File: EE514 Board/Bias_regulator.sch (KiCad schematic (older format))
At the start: 12 parts

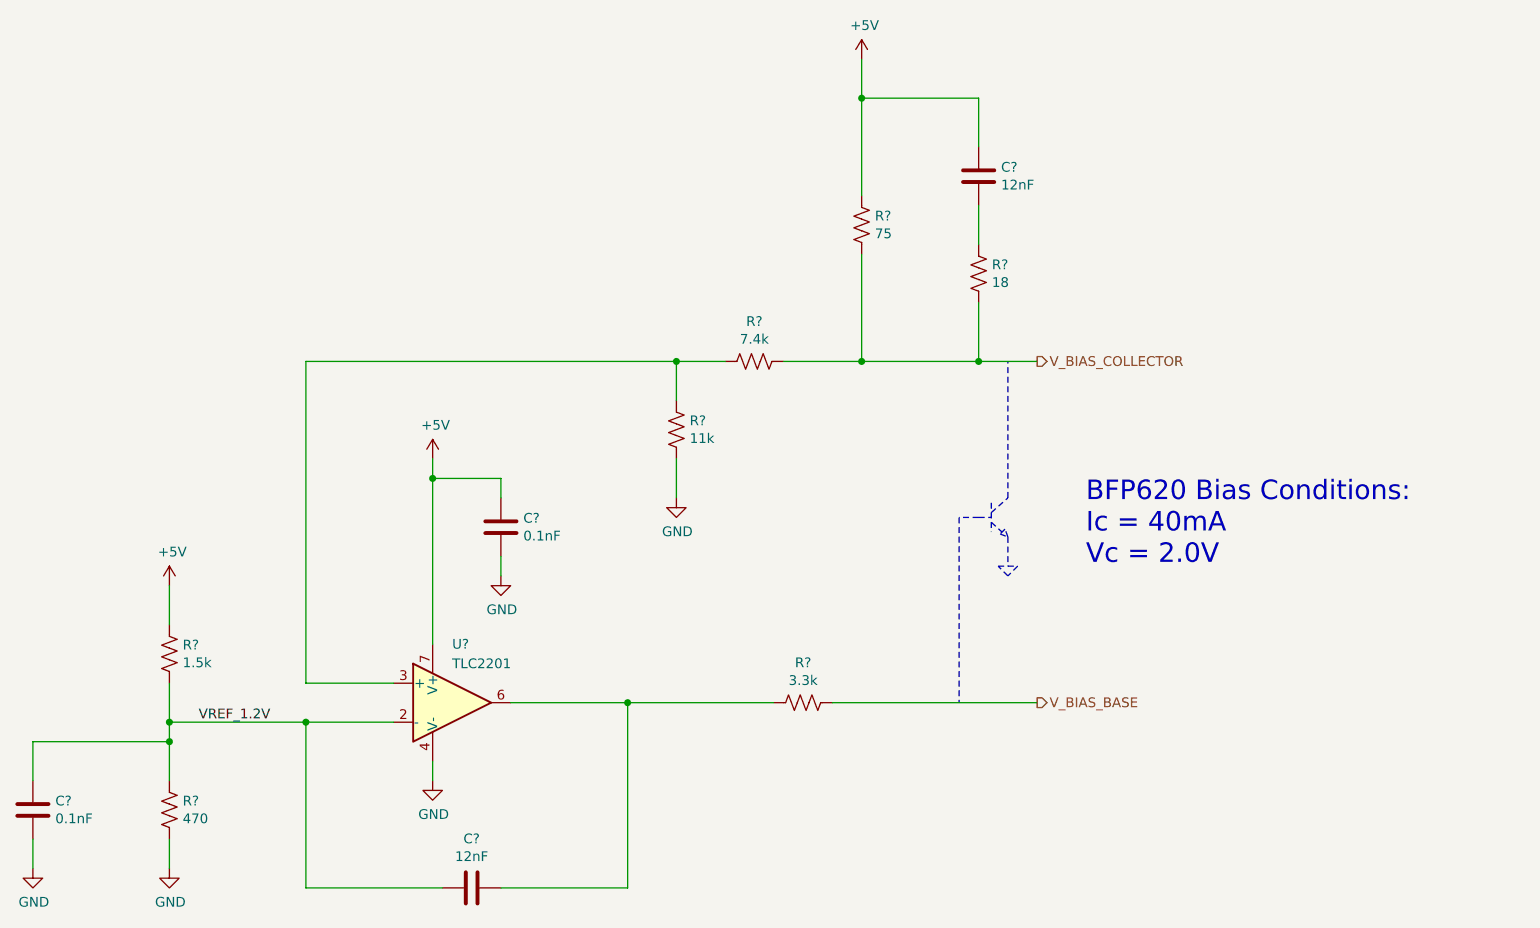
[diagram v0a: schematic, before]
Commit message: Layout finished, updating silkscreen...
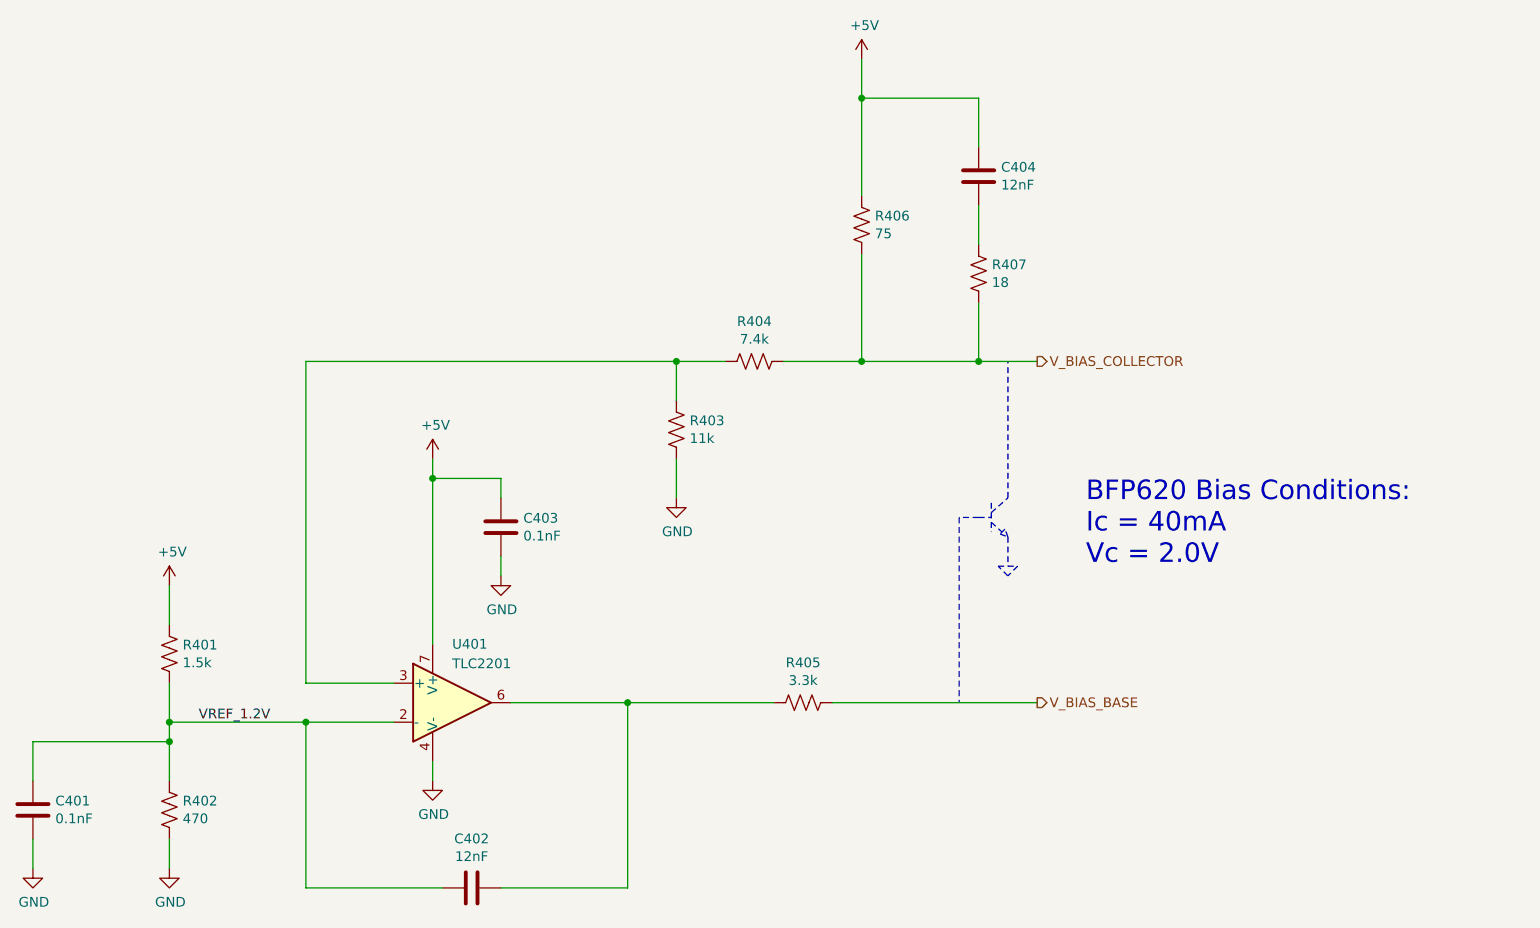
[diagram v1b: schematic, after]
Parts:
- C401, C402, C403, C404: renamed from C?; footprint (none) -> EE514 Board:C_0603_1608Metric_Pad0.98x0.95mm_HandSolder
- R401, R402, R403, R404, R405, R406, R407: renamed from R?; footprint (none) -> EE514 Board:R_0603_1608Metric_Pad0.98x0.95mm_HandSolder
- gave numbers to parts that had none: 1
